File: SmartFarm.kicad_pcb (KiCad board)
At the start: 2 copper layers, 80 x 80 mm, 31 parts, among them J1 Conn_01x20_Pin, J10 Conn_01x06_Socket, J11 Conn_01x06_Socket, J12 Conn_01x01_Pin, J13 Conn_01x01_Pin, J14 Conn_01x01_Pin, J15 Conn_01x01_Pin, J2 Conn_01x20_Pin, J3 Conn_01x06_Socket, J4 Conn_01x04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

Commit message: layout left
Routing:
- net /SCL: track 0.00 -> 97.7 mm, vias 0 -> 3
- net /SDA: track 0.00 -> 86.4 mm, vias 0 -> 1
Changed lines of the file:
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@@
     (effects (font (size 1 1) (thickness 0.15)) (justify left bottom))
   )
+  (segment (start 123.122644 110.592711) (end 115.467289 110.592711) (width 0.25) (layer "F.Cu") (net 31))
+  (segment (start 115.467289 110.592711) (end 105.41 120.65) (width 0.25) (layer "F.Cu") (net 31))
+  (segment (start 93.98 145.6) (end 93.98 132.08) (width 0.25) (layer "F.Cu") (net 31))
+  (segment (start 93.98 132.08) (end 96.52 129.54) (width 0.25) (layer "F.Cu") (net 31))
+  (segment (start 105.41 120.65) (end 105.41 121.92) (width 0.25) (layer "F.Cu") (net 31))
+  (segment (start 88.9 124.46) (end 88.9 123.19) (width 0.25) (layer "F.Cu") (net 31))
+  (segment (start 105.41 120.65) (end 96.52 129.54) (width 0.25) (layer "F.Cu") (net 31))
+  (segment (start 88.9 123.19) (end 90.17 121.92) (width 0.25) (layer "F.Cu") (net 31))
+  (segment (start 92.71 129.54) (end 78.74 129.54) (width 0.25) (layer "F.Cu") (net 31))
+  (segment (start 99.06 116.84) (end 99.06 118.11) (width 0.25) (layer "F.Cu") (net 31))
+  (segment (start 96.52 129.54) (end 92.71 129.54) (width 0.25) (layer "F.Cu") (net 31))
+  (segment (start 78.74 129.54) (end 76.2 132.08) (width 0.25) (layer "F.Cu") (net 31))
+  (segment (start 99.06 118.11) (end 100.33 119.38) (width 0.25) (layer "F.Cu") (net 31))
+  (via (at 90.17 121.92) (size 0.8) (drill 0.4) (layers "F.Cu" "B.Cu") (net 31))
+  (via (at 105.41 121.92) (size 0.8) (drill 0.4) (layers "F.Cu" "B.Cu") (net 31))
+  (via (at 100.33 119.38) (size 0.8) (drill 0.4) (layers "F.Cu" "B.Cu") (net 31))
+  (segment (start 97.79 121.92) (end 100.33 119.38) (width 0.25) (layer "B.Cu") (net 31))
+  (segment (start 90.17 121.92) (end 97.79 121.92) (width 0.25) (layer "B.Cu") (net 31))
+  (segment (start 105.41 121.92) (end 102.87 121.92) (width 0.25) (layer "B.Cu") (net 31))
+  (segment (start 102.87 121.92) (end 100.33 119.38) (width 0.25) (layer "B.Cu") (net 31))
+  (segment (start 105.41 119.38) (end 97.79 127) (width 0.25) (layer "F.Cu") (net 32))
+  (segment (start 104.14 119.38) (end 105.41 119.38) (width 0.25) (layer "F.Cu") (net 32))
+  (segment (start 124.918695 108.79666) (end 115.99334 108.79666) (width 0.25) (layer "F.Cu") (net 32))
+  (segment (start 86.36 124.46) (end 88.9 127) (width 0.25) (layer "F.Cu") (net 32))
+  (segment (start 97.79 127) (end 88.9 127) (width 0.25) (layer "F.Cu") (net 32))
+  (segment (start 101.6 116.84) (end 104.14 119.38) (width 0.25) (layer "F.Cu") (net 32))
+  (segment (start 88.9 127) (end 76.2 127) (width 0.25) (layer "F.Cu") (net 32))
+  (segment (start 97.79 127) (end 96.52 128.27) (width 0.25) (layer "F.Cu") (net 32))
+  (segment (start 96.52 128.27) (end 95.25 128.27) (width 0.25) (layer "F.Cu") (net 32))
+  (segment (start 115.99334 108.79666) (end 105.41 119.38) (width 0.25) (layer "F.Cu") (net 32))
+  (via (at 95.25 128.27) (size 0.8) (drill 0.4) (layers "F.Cu" "B.Cu") (net 32))
+  (segment (start 95.25 128.27) (end 94.93 128.27) (width 0.25) (layer "B.Cu") (net 32))
+  (segment (start 94.93 128.27) (end 94.5 128.7) (width 0.25) (layer "B.Cu") (net 32))
+  (segment (start 94.5 128.7) (end 94.5 142.2) (width 0.25) (layer "B.Cu") (net 32))
+  (segment (start 94.5 142.2) (end 96.52 144.22) (width 0.25) (layer "B.Cu") (net 32))
+  (segment (start 96.52 144.22) (end 96.52 145.6) (width 0.25) (layer "B.Cu") (net 32))
   (zone (net 19) (net_name "GND") (layer "F.Cu") (hatch edge 0.5)
     (connect_pads (clearance 0.5))

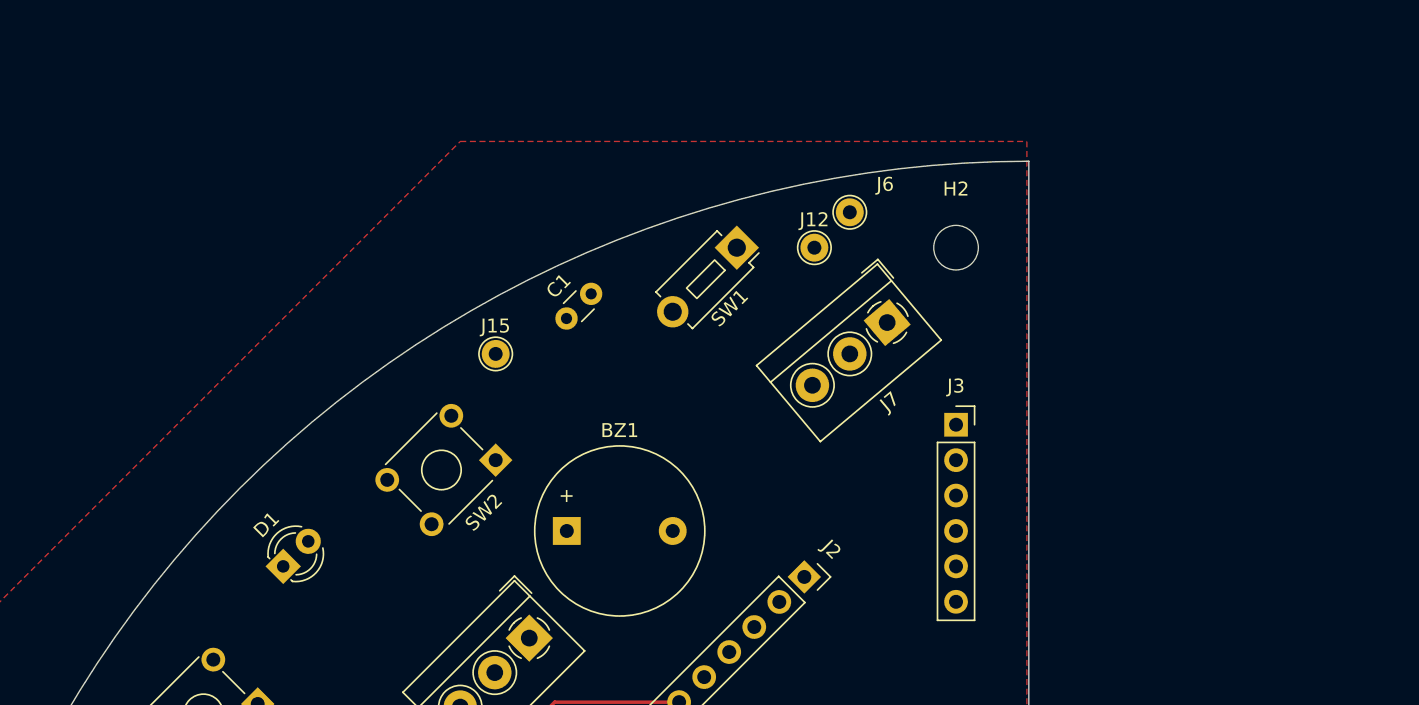
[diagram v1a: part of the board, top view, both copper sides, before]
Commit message: add potentialmeter and fan circuit
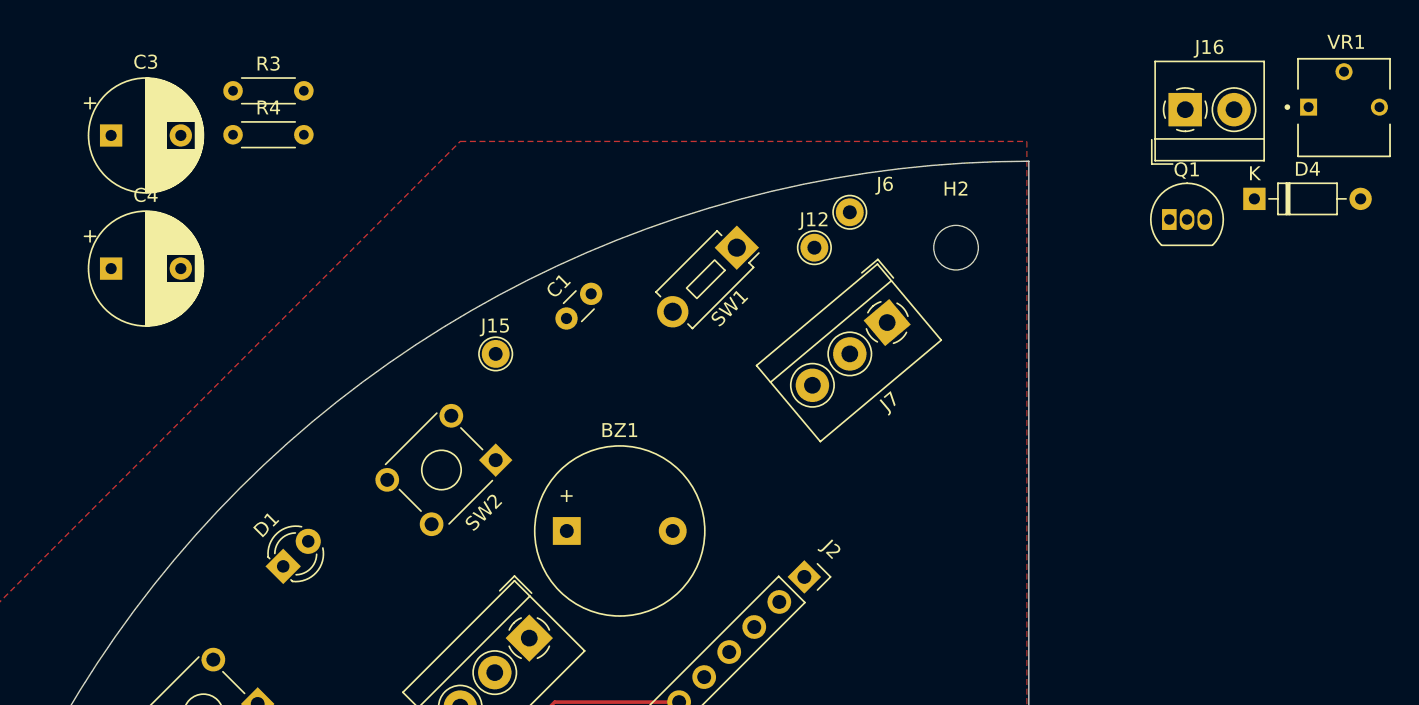
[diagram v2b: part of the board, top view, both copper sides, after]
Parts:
- removed J3: Conn_01x06_Socket, Connector_PinSocket_2.54mm:PinSocket_1x06_P2.54mm_Vertical
- added C3: 1000uF/10V, Capacitor_THT:CP_Radial_D8.0mm_P5.00mm, F.Cu at (84.2, 68.2)
- added C4: 1000uF/10V, Capacitor_THT:CP_Radial_D8.0mm_P5.00mm, F.Cu at (84.2, 77.7)
- added D4: 1N5712, Diode_THT:D_DO-35_SOD27_P7.62mm_Horizontal, F.Cu at (166.2, 72.7)
- added J16: Screw_Terminal_01x02, TerminalBlock_4Ucon:TerminalBlock_4Ucon_1x02_P3.50mm_Horizontal, F.Cu at (161.2, 66.3)
- added Q1: 2N3904, Package_TO_SOT_THT:TO-92_Inline, F.Cu at (160.1, 74.2)
- added R3: 220, Resistor_THT:R_Axial_DIN0204_L3.6mm_D1.6mm_P5.08mm_Horizontal, F.Cu at (92.9, 65.0)
- added R4: 220, Resistor_THT:R_Axial_DIN0204_L3.6mm_D1.6mm_P5.08mm_Horizontal, F.Cu at (92.9, 68.1)
- added VR1: 1K, 3362P-1-103:TRIM_3362P-1-103, F.Cu at (172.6, 66.1)
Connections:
- J1 pad 10: /A-1A -> /FAN
- J1 pad 14: /B-2A -> unconnected-(J1-Pin_14-Pad14)
- J1 pad 15: /B-1B -> unconnected-(J1-Pin_15-Pad15)
- J1 pad 9: /A-1B -> unconnected-(J1-Pin_9-Pad9)
- J7 pad 2: /DIN1 -> Net-(J7-Pin_2)
- J9 pad 2: /DIN2 -> Net-(J9-Pin_2)

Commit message: layout done
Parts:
- removed JP1: Jumper_2_Open, Jumper:SolderJumper-2_P1.3mm_Open_TrianglePad1.0x1.5mm
- added R5: 1k, Resistor_THT:R_Axial_DIN0204_L3.6mm_D1.6mm_P5.08mm_Horizontal, F.Cu at (142.9, 121.9)
- added R6: 4.7k, Resistor_THT:R_Axial_DIN0204_L3.6mm_D1.6mm_P5.08mm_Horizontal, F.Cu at (109.0, 99.7)
- D2, D4: footprint Diode_THT:D_DO-35_SOD27_P7.62mm_Horizontal -> Diode_THT:D_DO-35_SOD27_P10.16mm_Horizontal
- moved R4 74.2 mm to (87.8, 142.1)
- moved SW1 70.4 mm to (127.3, 146.6), turned to 0 degrees
- moved J15 58.6 mm to (104.6, 142.0)
- moved J6 51.1 mm to (139.2, 124.7)
- moved VR1 46.2 mm to (128.1, 78.6), turned to 90 degrees
- moved R1 44.1 mm to (99.6, 103.3), turned to 45 degrees
- moved R3 42.6 mm to (129.3, 87.0), turned to 180 degrees
- moved C4 40.3 mm to (84.4, 118.0), turned to 180 degrees
- moved D4 38.1 mm to (139.4, 99.8), turned to 90 degrees
- moved C3 34.8 mm to (115.6, 83.1)
- moved J16 33.2 mm to (145.6, 95.6), turned to 90 degrees
- moved J14 25.8 mm to (100.1, 141.7)
- moved D3 25.4 mm to (122.7, 140.7)
- moved J13 23.8 mm to (96.5, 139.4)
- moved Q1 17.3 mm to (147.5, 86.0), turned to 180 degrees
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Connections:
- BZ1 pad 1: GND -> /Buzz
- BZ1 pad 2: /Buzz -> GND
- J2 pad 10: /GP7 -> /Buzz
- J2 pad 12: /GP9 -> /LED
- J5 pad 3: +5V -> /3V3
- Q1 pad 2: /FAN -> Net-(Q1-B)
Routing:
- net /VSYS: track 0.00 -> 233.6 mm
- net /3V3: track 0.00 -> 133.4 mm
- net Net-(Q1-B): track 0.00 -> 43.8 mm
- net /Buzz: track 0.00 -> 36.9 mm
- net Net-(D4-K): track 0.00 -> 36.5 mm, vias 0 -> 1
- net /LED: track 0.00 -> 28.1 mm
- net /SW2: track 0.00 -> 27.1 mm
- net /SW1: track 0.00 -> 26.5 mm
- net /DIN1: track 0.00 -> 21.5 mm
- net /FAN: track 0.00 -> 17.7 mm
- net /DI: track 0.00 -> 17.6 mm
- net /RUN: track 0.00 -> 17.3 mm
- net Net-(D2-A): track 0.00 -> 16.8 mm
- net Net-(J7-Pin_2): track 0.00 -> 14.2 mm
- net /DIN2: track 0.00 -> 13.8 mm
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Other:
- board text added: "+"
- board text added: "+5V"
- board text added: "-"
- board text added: "3V3"
- board text added: "B"
- board text added: "C"
- board text added: "DIN"
- board text added: "E"
- board text added: "GND"
- board text added: "VSYS"

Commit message: sample
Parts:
- moved G*** 1.90 mm to (118.2, 118.2)
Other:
- board text added: "DI"
- board text added: "RTC Display Temperature/Humidity Waterproof Temperature Neopixel FAN Buzzer"
- board text added: "SmartFarm Ver0_1"
- board text added: "X"
- board text added: "https://github.com/microschool-kr/Microschool-DataPi-SmartFarm"
- board text removed: "+5V"
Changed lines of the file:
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@@
     (property "ki_keywords" "screw terminal")
     (attr through_hole)
-    (fp_text reference "J5" (at 3.5 -4.46 45) (layer "F.SilkS")
+    (fp_text reference "J5" (at 10.298742 -2.421931 45) (layer "F.SilkS")
         (effects (font (size 1 1) (thickness 0.15)))
     )
@@
   )
   (footprint "SmartFarm:DataPi_logo" (layer "B.Cu")
-    (at 120.005621 117.592958 45)
+    (at 118.2 118.2 45)
     (attr board_only exclude_from_pos_files exclude_from_bom)
     (fp_text reference "G***" (at 0 0 45) (layer "B.SilkS") hide
@@
   (gr_arc (start 70 150) (mid 93.431458 93.431458) (end 150 70)
     (stroke (width 0.1) (type default)) (layer "Edge.Cuts"))
-  (gr_text "C" (at 144.1 83.7) (layer "F.SilkS")
+  (gr_text "https://github.com/microschool-kr/Microschool-DataPi-SmartFarm" (at 148.1 123.5 270) (layer "B.SilkS")
+    (effects (font (size 1 1) (thickness 0.25) bold) (justify left bottom mirror))
+  )
+  (gr_text "SmartFarm Ver0_1" (at 79.4 147.7 180) (layer "B.SilkS")
+    (effects (font (size 1.5 1.5) (thickness 0.25) bold) (justify left bottom mirror))
+  )
+  (gr_text "RTC \nDisplay \nTemperature/Humidity \nWaterproof Temperature \nNeopixel \nFAN \nBuzzer " (at 85.2 104.6 225) (layer "B.SilkS")
+    (effects (font (size 1.5 1.5) (thickness 0.375) bold) (justify left bottom mirror))
+  )
+  (gr_text "C" (at 144 83.7) (layer "F.SilkS")
+    (effects (font (size 1 1) (thickness 0.2) bold) (justify left bottom))
+  )
+  (gr_text "X" (at 101.8 149) (layer "F.SilkS")
     (effects (font (size 1 1) (thickness 0.2) bold) (justify left bottom))
   )
@@
     (effects (font (size 1 1) (thickness 0.2) bold) (justify left bottom))
   )
-  (gr_text "3V3" (at 82.3 127.7) (layer "F.SilkS")
+  (gr_text "3V3" (at 82.400952 127.7) (layer "F.SilkS")
     (effects (font (size 1 1) (thickness 0.2) bold) (justify left bottom))
   )
@@
     (effects (font (size 1 1) (thickness 0.2) bold) (justify left bottom))
   )
-  (gr_text "SCL" (at 98.2 114.6) (layer "F.SilkS")
+  (gr_text "SCL" (at 97.9 120.3) (layer "F.SilkS")
+    (effects (font (size 1 1) (thickness 0.2) bold) (justify left bottom))
+  )
+  (gr_text "DI" (at 115.2 109 -135) (layer "F.SilkS")
     (effects (font (size 1 1) (thickness 0.2) bold) (justify left bottom))
   )
@@
     (effects (font (size 1 1) (thickness 0.2) bold) (justify left bottom))
   )
-  (gr_text "SDA\n\n" (at 85.4 129.31) (layer "F.SilkS")
+  (gr_text "SDA\n" (at 85.61619 127.7) (layer "F.SilkS")
     (effects (font (size 1 1) (thickness 0.2) bold) (justify left bottom))
   )
-  (gr_text "GND\n" (at 86.3 148.99) (layer "F.SilkS")
+  (gr_text "GND\n" (at 87.1 149) (layer "F.SilkS")
     (effects (font (size 1 1) (thickness 0.2) bold) (justify left bottom))
   )
-  (gr_text "+5V" (at 78.2 132.8 225) (layer "F.SilkS")
+  (gr_text "X" (at 93.5 127.7) (layer "F.SilkS")
     (effects (font (size 1 1) (thickness 0.2) bold) (justify left bottom))
   )
@@
     (effects (font (size 1 1) (thickness 0.2) bold) (justify left bottom))
   )
-  (gr_text "3V3" (at 91.9 114.6) (layer "F.SilkS")
+  (gr_text "GND\n" (at 84.4 128.7 -140) (layer "F.SilkS")
+    (effects (font (size 1 1) (thickness 0.2) bold) (justify left bottom))
+  )
+  (gr_text "3V3" (at 91.6 120.3) (layer "F.SilkS")
+    (effects (font (size 1 1) (thickness 0.2) bold) (justify left bottom))
+  )
+  (gr_text "3V3" (at 113.634264 110.565737 -135) (layer "F.SilkS")
+    (effects (font (size 1 1) (thickness 0.2) bold) (justify left bottom))
+  )
+  (gr_text " DIN" (at 81.93533 130.7 220) (layer "F.SilkS")
     (effects (font (size 1 1) (thickness 0.2) bold) (justify left bottom))
   )
@@
     (effects (font (size 1 1) (thickness 0.2) bold) (justify left bottom))
   )
-  (gr_text "+5V" (at 129.8 82.3 225) (layer "F.SilkS")
+  (gr_text "  VSYS" (at 135.664671 77.9 219) (layer "F.SilkS")
     (effects (font (size 1 1) (thickness 0.2) bold) (justify left bottom))
   )
@@
     (effects (font (size 1 1) (thickness 0.2) bold) (justify left bottom))
   )
-  (gr_text "GND\n" (at 137.8 75.7 225) (layer "F.SilkS")
+  (gr_text "GND\n" (at 140.16467 74.2 220) (layer "F.SilkS")
     (effects (font (size 1 1) (thickness 0.2) bold) (justify left bottom))
   )
-  (gr_text "SDA\n\n" (at 95.9 150.6) (layer "F.SilkS")
+  (gr_text "SDA" (at 97.091428 149) (layer "F.SilkS")
     (effects (font (size 1 1) (thickness 0.2) bold) (justify left bottom))
   )
-  (gr_text "SCL" (at 88.5 127.7) (layer "F.SilkS")
+  (gr_text "SCL" (at 88.879047 127.7) (layer "F.SilkS")
     (effects (font (size 1 1) (thickness 0.2) bold) (justify left bottom))
   )
-  (gr_text "SDA" (at 101.2 114.6) (layer "F.SilkS")
+  (gr_text "SDA" (at 100.9 120.3) (layer "F.SilkS")
     (effects (font (size 1 1) (thickness 0.2) bold) (justify left bottom))
   )
@@
     (effects (font (size 1 1) (thickness 0.2) bold) (justify left bottom))
   )
-  (gr_text "B\n" (at 145.7 83.7) (layer "F.SilkS")
+  (gr_text "B\n" (at 145.6 83.7) (layer "F.SilkS")
     (effects (font (size 1 1) (thickness 0.2) bold) (justify left bottom))
   )
-  (gr_text "3V3" (at 89.7 148.99) (layer "F.SilkS")
+  (gr_text "3V3" (at 90.620952 149) (layer "F.SilkS")
     (effects (font (size 1 1) (thickness 0.2) bold) (justify left bottom))
   )
@@
     (effects (font (size 1 1) (thickness 0.2) bold) (justify left bottom))
   )
-  (gr_text "SCL" (at 92.8 148.99) (layer "F.SilkS")
+  (gr_text "SCL" (at 93.85619 149) (layer "F.SilkS")
+    (effects (font (size 1 1) (thickness 0.2) bold) (justify left bottom))
+  )
+  (gr_text " DIN " (at 137.7 76.2 220) (layer "F.SilkS")
     (effects (font (size 1 1) (thickness 0.2) bold) (justify left bottom))
   )
-  (gr_text "DIN" (at 80.7 130.4 225) (layer "F.SilkS")
+  (gr_text "GND" (at 117.876904 106.323096 -135) (layer "F.SilkS")
     (effects (font (size 1 1) (thickness 0.2) bold) (justify left bottom))
   )
-  (gr_text "DIN" (at 135.1 78 225) (layer "F.SilkS")
+  (gr_text "GND\n" (at 94.7 120.3) (layer "F.SilkS")
     (effects (font (size 1 1) (thickness 0.2) bold) (justify left bottom))
   )
-  (gr_text "GND\n" (at 95 114.6) (layer "F.SilkS")
+  (gr_text "X" (at 92.094285 127.7) (layer "F.SilkS")
     (effects (font (size 1 1) (thickness 0.2) bold) (justify left bottom))
   )
-  (gr_text "GND\n" (at 83.5 127.9 225) (layer "F.SilkS")
+  (gr_text "  VSYS" (at 79.900001 132.4 219) (layer "F.SilkS")
     (effects (font (size 1 1) (thickness 0.2) bold) (justify left bottom))
   )
-  (gr_text "E\n" (at 147.3 83.7) (layer "F.SilkS")
+  (gr_text "X" (at 100.374285 149) (layer "F.SilkS")
+    (effects (font (size 1 1) (thickness 0.2) bold) (justify left bottom))
+  )
+  (gr_text "E\n" (at 147.2 83.7) (layer "F.SilkS")
     (effects (font (size 1 1) (thickness 0.2) bold) (justify left bottom))
   )
@@
     )
   )
+  (group "" (id 1084edde-f3f1-4d8c-898d-2b8c7fcc1b30)
+    (members
+      0d28ffe8-a1ac-49fb-ba1f-d56efd3547b3
+      43814e9e-a5ea-41b7-b618-799114d2db62
+      a8b6abee-9311-4444-9a63-9b853bd62d28
+      b78016b6-98a1-4cff-9074-cb6c37c90929
+      bcdb17fb-edf2-4665-a171-3034177daf18
+      f6b7066c-82c0-43c6-8376-d1bc8b38d7bf
+    )
+  )
+  (group "" (id 2b3e1401-4ae9-4c5d-8342-5986a1d60f79)
+    (members
+      90ebcbbf-beed-460a-b2aa-867c9d9da6d0
+      98ca5a03-1206-4a12-9114-e89ec3cd5f63
+      d475187a-2c5e-4b95-8251-d9647a672183
+    )
+  )
+  (group "" (id 2be72e8b-e996-4030-86d0-95d42d1815b6)
+    (members
+      000d6840-99fd-4e12-9e7f-ac4f8af7719a
+      b674789d-d842-4b16-871f-4ac031cbc629
+      f6d96ebb-c94a-4dda-9ba4-04efd616d695
+    )
+  )
+  (group "" (id 4daaa5e9-ca60-456a-8d21-ac07844b0c57)
+    (members
+      6ceb2e22-2c26-4a02-a519-ca7caa4cc29e
+      7a36083e-8a5a-4da7-98a2-3eb2d6373030
+      efc0b6ee-a587-4258-8332-2e46f75c0704
+    )
+  )
+  (group "" (id 57303caf-1107-4a77-a6ba-5fb02ad3d7a8)
+    (members
+      3478c00f-95e3-4cec-8b6f-91ae5654d609
+      6d976daa-3432-4cba-9156-88f624c2db86
+      b0a34b33-61e3-4f64-b34c-07071b432fea
+      e38a02d1-6612-42fb-bb94-e128594dd435
+    )
+  )
+  (group "" (id a9bac886-cb57-402d-9aaa-7d9b474bd885)
+    (members
+      186e3389-5b5a-4136-ad65-19f960182c5d
+      18701722-d67b-4a63-9285-2daf15c9b006
+      396a7da0-7d66-4381-8749-f667035e460a
+      578edf73-b6a2-4201-a4e7-e61c3f3920dd
+      aaa83592-4845-4f3a-8f85-1ba9f8fb2b8c
+      ef493082-6db1-4090-b221-fc78f2fb06cb
+    )
+  )
+  (group "" (id c3ea8b2b-14a3-46cd-9b84-d6ff783036db)
+    (members
+      35ea606f-1e84-49f1-b0a4-2f1637fbb932
+      752f6995-c6e0-49d3-9b8c-f18c8c4fcd51
+      dd36d0c8-5b1b-46a2-aefa-1ceef3e1214f
+    )
+  )
